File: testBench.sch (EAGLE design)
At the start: 29 parts, among them IC1 NCS21911SN2T1G, IC2 NCS21911SN2T1G, IC3 NCS21911SN2T1G, IC4 NCS21911SN2T1G, IC5 NCS21911SN2T1G

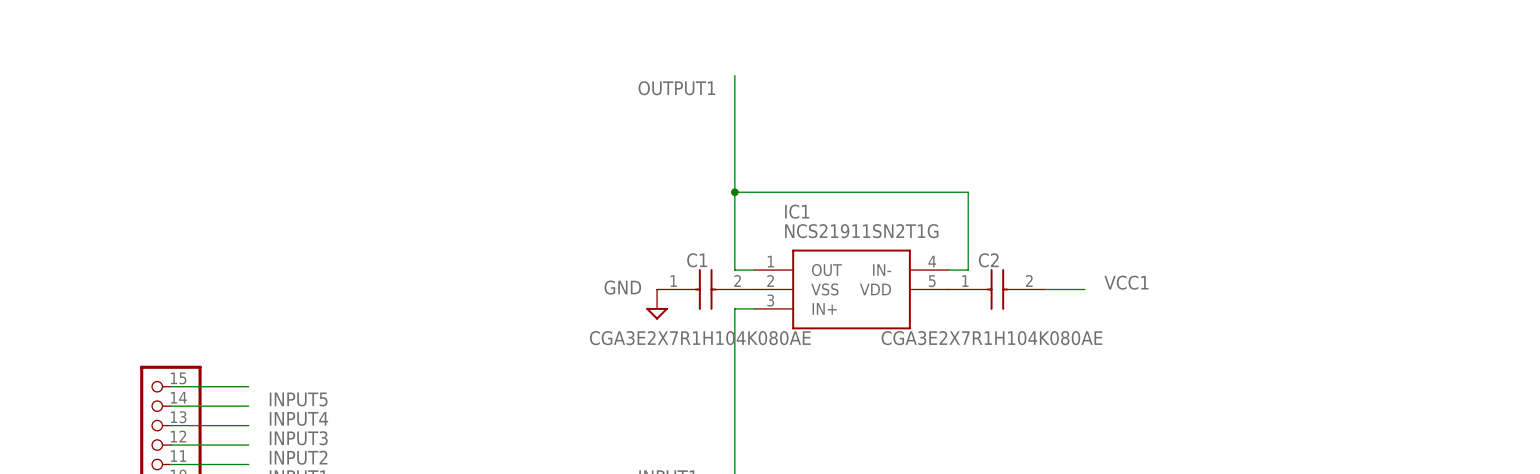
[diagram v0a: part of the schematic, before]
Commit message: Added comments on schematics
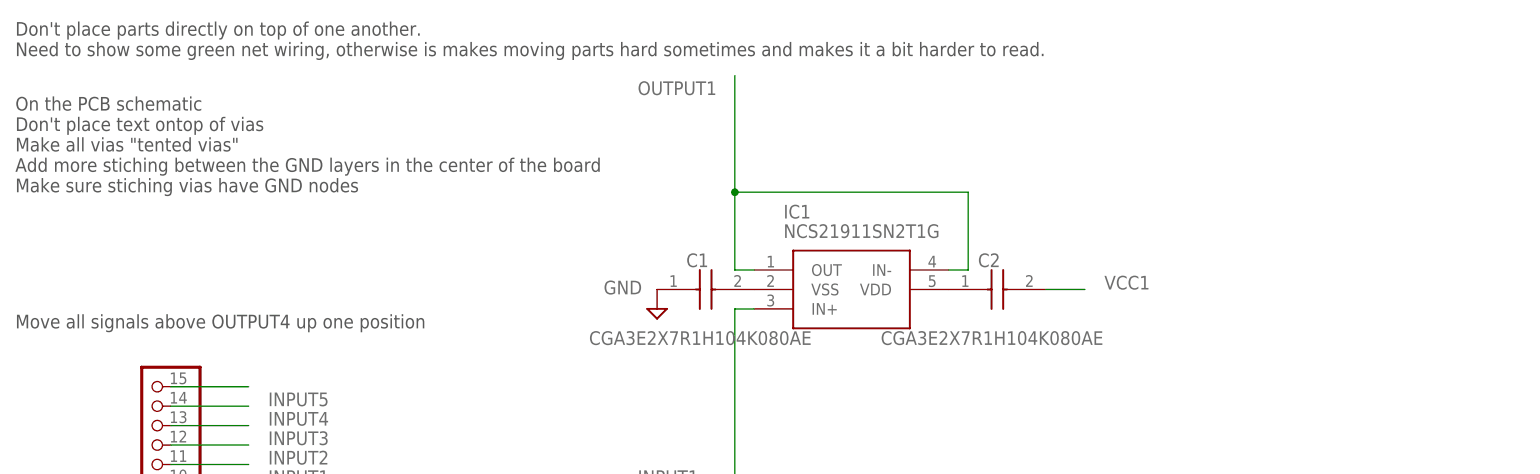
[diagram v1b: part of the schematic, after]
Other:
- note added: "Don't place parts directly on top of one another. Need to show some green net wiring, otherwise is makes moving parts hard sometimes and makes it a bit harder to read."
- note added: "Move all signals above OUTPUT4 up one position"
- note added: "On the PCB schematic Don't place text ontop of vias Make all vias "tented vias" Add more stiching between the GND layers in the center of the board Make sure stiching vias have GND nodes"
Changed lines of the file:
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@@
 <text x="124.46" y="-104.14" size="5.08" layer="97">Second-order Low-pass Filter</text>
 <text x="124.46" y="-238.76" size="5.08" layer="97">Differential Amplifier</text>
+<text x="-127" y="30.48" size="1.778" layer="97">Move all signals above OUTPUT4 up one position</text>
+<text x="-127" y="66.04" size="1.778" layer="97">Don't place parts directly on top of one another.
+Need to show some green net wiring, otherwise is makes moving parts hard sometimes and makes it a bit harder to read.</text>
+<text x="-127" y="48.26" size="1.778" layer="97">On the PCB schematic
+Don't place text ontop of vias
+Make all vias "tented vias"
+Add more stiching between the GND layers in the center of the board
+Make sure stiching vias have GND nodes</text>
 </plain>
 <instances>
@@
 </drawing>
 <compatibility>
+<note version="6.3" minversion="6.2.2" severity="warning">
+Since Version 6.2.2 text objects can contain more than one line,
+which will not be processed correctly with this version.
+</note>
 <note version="8.2" severity="warning">
 Since Version 8.2, EAGLE supports online libraries. The ids

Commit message: This is my third PCB for opamp test bench
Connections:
- removed net N$44: JP3.15
- new net EMPTY: JP3.5
- net GND: now also JP3.10; no longer JP3.9
- net INPUT1: now also JP3.11; no longer JP3.10
- net INPUT2: now also JP3.12; no longer JP3.11
- net INPUT3: now also JP3.13; no longer JP3.12
- net INPUT4: now also JP3.14; no longer JP3.13
- net INPUT5: now also JP3.15; no longer JP3.14
- net VCC1: now also JP3.6; no longer JP3.5
- net VCC2: now also JP3.7; no longer JP3.6
- net VCC3: now also JP3.8; no longer JP3.7
- net VCC4: now also JP3.9; no longer JP3.8
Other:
- moved on the sheet: C1, C10, C11, C12, C13, C2, C3, C4, C6, C7

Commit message: PCB test bench fourth version
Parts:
- removed C1, C10, C12, C3, C6: CGA3E2X7R1H104K080AE, SamacSys_Parts:CGA3E2X7R1H104K080AE
- added TP1, TP2, TP3, TP4, TP5, TP6, TP7, TP8: (no value), SamacSys_Parts:S1751-46R
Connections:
- removed net N$16: C11.1, IC5.VDD
- removed net N$17: C10.2, IC5.VSS
- removed net N$2: C1.2, IC1.VSS
- removed net N$3: C2.1, IC1.VDD
- removed net N$4: C3.2, IC2.VSS
- removed net N$5: C4.1, IC2.VDD
- removed net N$6: C6.2, IC3.VSS
- removed net N$7: C7.1, IC3.VDD
- removed net N$8: C13.1, IC4.VDD
- removed net N$9: C12.2, IC4.VSS
- net GND: now also C11.2, C13.2, C2.2, C4.2, C7.2, IC1.VSS, IC2.VSS, IC3.VSS, IC4.VSS, IC5.VSS, TP1.TP, TP3.TP, TP5.TP, TP7.TP; no longer C1.1, C10.1, C12.1, C3.1, C6.1
- net OUTPUT1: now also TP2.TP
- net OUTPUT2: now also TP4.TP
- net OUTPUT3: now also TP6.TP
- net OUTPUT4: now also TP8.TP
- net VCC1: now also C2.1, IC1.VDD; no longer C2.2
- net VCC2: now also C4.1, IC2.VDD; no longer C4.2
- net VCC3: now also C11.1, C7.1, IC3.VDD, IC5.VDD; no longer C11.2, C7.2
- net VCC4: now also C13.1, IC4.VDD; no longer C13.2
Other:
- moved on the sheet: C11, C13, C2, C4, C7, C8

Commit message: pcb test bench 6th version
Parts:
- removed R6: CRCW080510M0FKEB, SamacSys_Parts:CRCW080510M0FKEB
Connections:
- removed net N$18: IC5.OUT, R6.1, R7.1
- net OUTPUT3: now also IC5.OUT, R7.1; no longer R6.2
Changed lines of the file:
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@@
 <part name="C11" library="SamacSys_Parts" deviceset="CGA3E2X7R1H104K080AE" device=""/>
 <part name="SUPPLY10" library="supply2" library_urn="urn:adsk.eagle:library:372" deviceset="GND" device=""/>
-<part name="R6" library="SamacSys_Parts" deviceset="CRCW080510M0FKEB" device=""/>
 <part name="SUPPLY13" library="supply2" library_urn="urn:adsk.eagle:library:372" deviceset="GND" device=""/>
 <part name="R8" library="SamacSys_Parts" deviceset="TNPW080510K0BEEN" device=""/>
@@
 <attribute name="VALUE" x="36.195" y="-140.335" size="1.778" layer="96"/>
 </instance>
-<instance part="R6" gate="G$1" x="43.18" y="-93.98" smashed="yes" rot="R90">
-<attribute name="NAME" x="36.83" y="-82.55" size="1.778" layer="95" rot="R180" align="center-left"/>
-<attribute name="VALUE" x="39.37" y="-87.63" size="1.778" layer="96" rot="R180" align="center-left"/>
-</instance>
 <instance part="SUPPLY13" gate="GND" x="-5.08" y="-139.7" smashed="yes" rot="R90">
 <attribute name="VALUE" x="1.905" y="-139.065" size="1.778" layer="96" rot="R180"/>
@@
 </segment>
 </net>
-<net name="N$18" class="0">
-<segment>
+<net name="OUTPUT3" class="0">
+<segment>
+<label x="48.26" y="-66.04" size="1.778" layer="95" rot="R180"/>
 <pinref part="IC5" gate="G$1" pin="OUT"/>
-<pinref part="R6" gate="G$1" pin="1"/>
 <wire x1="43.18" y1="-121.92" x2="43.18" y2="-104.14" width="0.1524" layer="91"/>
 <pinref part="R7" gate="G$1" pin="1"/>
-<wire x1="43.18" y1="-104.14" x2="43.18" y2="-93.98" width="0.1524" layer="91"/>
 <wire x1="43.18" y1="-104.14" x2="45.72" y2="-104.14" width="0.1524" layer="91"/>
 <junction x="43.18" y="-104.14"/>
-</segment>
-</net>
-<net name="OUTPUT3" class="0">
-<segment>
-<pinref part="R6" gate="G$1" pin="2"/>
-<wire x1="43.18" y1="-76.2" x2="43.18" y2="-71.12" width="0.1524" layer="91"/>
-<label x="48.26" y="-66.04" size="1.778" layer="95" rot="R180"/>
-</segment>
-<segment>
+<wire x1="43.18" y1="-71.12" x2="43.18" y2="-104.14" width="0.1524" layer="91"/>
+</segment>
+<segment>

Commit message: PCB test bench version 8th
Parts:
- added LED1, LED2, LED3, LED4: 150080GS75000, SamacSys_Parts:150080GS75000
- added R13, R14, R15, R16: ERJ-P06J431V, SamacSys_Parts:ERJ-P06J431V
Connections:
- new net N$23: LED1.A, R13.2
- new net N$30: LED2.A, R14.2
- new net N$31: LED3.A, R15.2
- new net N$32: LED4.A, R16.2
- net GND: now also LED1.K, LED2.K, LED3.K, LED4.K
- net VCC1: now also R13.1
- net VCC2: now also R14.1
- net VCC3: now also R15.1
- net VCC4: now also R16.1
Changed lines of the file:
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@@
 <part name="TP7" library="SamacSys_Parts" deviceset="S1751-46R" device=""/>
 <part name="TP8" library="SamacSys_Parts" deviceset="S1751-46R" device=""/>
+<part name="LED1" library="SamacSys_Parts" deviceset="150080GS75000" device=""/>
+<part name="R13" library="SamacSys_Parts" deviceset="ERJ-P06J431V" device=""/>
+<part name="SUPPLY15" library="supply2" library_urn="urn:adsk.eagle:library:372" deviceset="GND" device=""/>
+<part name="LED2" library="SamacSys_Parts" deviceset="150080GS75000" device=""/>
+<part name="R14" library="SamacSys_Parts" deviceset="ERJ-P06J431V" device=""/>
+<part name="SUPPLY16" library="supply2" library_urn="urn:adsk.eagle:library:372" deviceset="GND" device=""/>
+<part name="LED3" library="SamacSys_Parts" deviceset="150080GS75000" device=""/>
+<part name="R15" library="SamacSys_Parts" deviceset="ERJ-P06J431V" device=""/>
+<part name="SUPPLY17" library="supply2" library_urn="urn:adsk.eagle:library:372" deviceset="GND" device=""/>
+<part name="LED4" library="SamacSys_Parts" deviceset="150080GS75000" device=""/>
+<part name="R16" library="SamacSys_Parts" deviceset="ERJ-P06J431V" device=""/>
+<part name="SUPPLY18" library="supply2" library_urn="urn:adsk.eagle:library:372" deviceset="GND" device=""/>
 </parts>
 <sheets>
@@
 <attribute name="NAME" x="53.34" y="-256.54" size="1.27" layer="95" rot="R270"/>
 </instance>
+<instance part="LED1" gate="G$1" x="-172.72" y="22.86" smashed="yes" rot="R180">
+<attribute name="NAME" x="-167.64" y="31.75" size="1.778" layer="95" rot="R180"/>
+<attribute name="VALUE" x="-167.64" y="29.21" size="1.778" layer="96" rot="R180"/>
+</instance>
+<instance part="R13" gate="G$1" x="-220.98" y="22.86" smashed="yes">
+<attribute name="NAME" x="-207.01" y="29.21" size="1.778" layer="95" align="center-left"/>
+<attribute name="VALUE" x="-207.01" y="26.67" size="1.778" layer="96" align="center-left"/>
+</instance>
+<instance part="SUPPLY15" gate="GND" x="-157.48" y="22.86" smashed="yes" rot="R90">
+<attribute name="VALUE" x="-150.495" y="23.495" size="1.778" layer="96" rot="R180"/>
+</instance>
+<instance part="LED2" gate="G$1" x="-172.72" y="10.16" smashed="yes" rot="R180">
+<attribute name="NAME" x="-167.64" y="19.05" size="1.778" layer="95" rot="R180"/>
+<attribute name="VALUE" x="-167.64" y="16.51" size="1.778" layer="96" rot="R180"/>
+</instance>
+<instance part="R14" gate="G$1" x="-220.98" y="10.16" smashed="yes">
+<attribute name="NAME" x="-207.01" y="16.51" size="1.778" layer="95" align="center-left"/>
+<attribute name="VALUE" x="-207.01" y="13.97" size="1.778" layer="96" align="center-left"/>
+</instance>
+<instance part="SUPPLY16" gate="GND" x="-157.48" y="10.16" smashed="yes" rot="R90">
+<attribute name="VALUE" x="-150.495" y="10.795" size="1.778" layer="96" rot="R180"/>
+</instance>
+<instance part="LED3" gate="G$1" x="-172.72" y="-2.54" smashed="yes" rot="R180">
+<attribute name="NAME" x="-167.64" y="6.35" size="1.778" layer="95" rot="R180"/>
+<attribute name="VALUE" x="-167.64" y="3.81" size="1.778" layer="96" rot="R180"/>
+</instance>
+<instance part="R15" gate="G$1" x="-220.98" y="-2.54" smashed="yes">
+<attribute name="NAME" x="-207.01" y="3.81" size="1.778" layer="95" align="center-left"/>
+<attribute name="VALUE" x="-207.01" y="1.27" size="1.778" layer="96" align="center-left"/>
+</instance>
+<instance part="SUPPLY17" gate="GND" x="-157.48" y="-2.54" smashed="yes" rot="R90">
+<attribute name="VALUE" x="-150.495" y="-1.905" size="1.778" layer="96" rot="R180"/>
+</instance>
+<instance part="LED4" gate="G$1" x="-172.72" y="-15.24" smashed="yes" rot="R180">
+<attribute name="NAME" x="-167.64" y="-6.35" size="1.778" layer="95" rot="R180"/>
+<attribute name="VALUE" x="-167.64" y="-8.89" size="1.778" layer="96" rot="R180"/>
+</instance>
+<instance part="R16" gate="G$1" x="-220.98" y="-15.24" smashed="yes">
+<attribute name="NAME" x="-207.01" y="-8.89" size="1.778" layer="95" align="center-left"/>
+<attribute name="VALUE" x="-207.01" y="-11.43" size="1.778" layer="96" align="center-left"/>
+</instance>
+<instance part="SUPPLY18" gate="GND" x="-157.48" y="-15.24" smashed="yes" rot="R90">
+<attribute name="VALUE" x="-150.495" y="-14.605" size="1.778" layer="96" rot="R180"/>
+</instance>
 </instances>
 <busses>
@@
 <wire x1="68.58" y1="-243.84" x2="76.2" y2="-243.84" width="0.1524" layer="91"/>
 <label x="78.74" y="-243.84" size="1.778" layer="95"/>
+</segment>
+<segment>
+<pinref part="LED1" gate="G$1" pin="K"/>
+<wire x1="-172.72" y1="22.86" x2="-160.02" y2="22.86" width="0.1524" layer="91"/>
+<pinref part="SUPPLY15" gate="GND" pin="GND"/>
+</segment>
+<segment>
+<pinref part="LED2" gate="G$1" pin="K"/>
+<wire x1="-172.72" y1="10.16" x2="-160.02" y2="10.16" width="0.1524" layer="91"/>
+<pinref part="SUPPLY16" gate="GND" pin="GND"/>
+</segment>
+<segment>
+<pinref part="LED3" gate="G$1" pin="K"/>
+<wire x1="-172.72" y1="-2.54" x2="-160.02" y2="-2.54" width="0.1524" layer="91"/>
+<pinref part="SUPPLY17" gate="GND" pin="GND"/>
+</segment>
+<segment>
+<pinref part="LED4" gate="G$1" pin="K"/>
+<wire x1="-172.72" y1="-15.24" x2="-160.02" y2="-15.24" width="0.1524" layer="91"/>
+<pinref part="SUPPLY18" gate="GND" pin="GND"/>
 </segment>
 </net>
@@
 <label x="25.4" y="-233.68" size="1.778" layer="95"/>
 </segment>
+<segment>
+<pinref part="R16" gate="G$1" pin="1"/>
+<wire x1="-220.98" y1="-15.24" x2="-233.68" y2="-15.24" width="0.1524" layer="91"/>
+<label x="-241.3" y="-15.24" size="1.778" layer="95"/>
+</segment>
 </net>
 <net name="VCC3" class="0">
@@
 <label x="10.16" y="-124.46" size="1.778" layer="95"/>
 </segment>
+<segment>
+<pinref part="R15" gate="G$1" pin="1"/>
+<wire x1="-220.98" y1="-2.54" x2="-233.68" y2="-2.54" width="0.1524" layer="91"/>
+<label x="-241.3" y="-2.54" size="1.778" layer="95"/>
+</segment>
 </net>
 <net name="VCC2" class="0">
@@
 <label x="22.86" y="-30.48" size="1.778" layer="95"/>
 </segment>
+<segment>
+<pinref part="R14" gate="G$1" pin="1"/>
+<wire x1="-220.98" y1="10.16" x2="-233.68" y2="10.16" width="0.1524" layer="91"/>
+<label x="-241.3" y="10.16" size="1.778" layer="95"/>
+</segment>
 </net>
 <net name="VCC1" class="0">
@@
 <label x="15.24" y="35.56" size="1.778" layer="95"/>
 </segment>
+<segment>
+<pinref part="R13" gate="G$1" pin="1"/>
+<wire x1="-220.98" y1="22.86" x2="-233.68" y2="22.86" width="0.1524" layer="91"/>
+<label x="-241.3" y="22.86" size="1.778" layer="95"/>
+</segment>
 </net>
 <net name="EMPTY" class="0">
@@
 </segment>
 </net>
+<net name="N$23" class="0">
+<segment>
+<pinref part="R13" gate="G$1" pin="2"/>
+<pinref part="LED1" gate="G$1" pin="A"/>
+<wire x1="-203.2" y1="22.86" x2="-187.96" y2="22.86" width="0.1524" layer="91"/>
+</segment>
+</net>
+<net name="N$30" class="0">
+<segment>
+<pinref part="R14" gate="G$1" pin="2"/>
+<pinref part="LED2" gate="G$1" pin="A"/>
+<wire x1="-203.2" y1="10.16" x2="-187.96" y2="10.16" width="0.1524" layer="91"/>
+</segment>
+</net>
+<net name="N$31" class="0">
+<segment>
+<pinref part="R15" gate="G$1" pin="2"/>
+<pinref part="LED3" gate="G$1" pin="A"/>
+<wire x1="-203.2" y1="-2.54" x2="-187.96" y2="-2.54" width="0.1524" layer="91"/>
+</segment>
+</net>
+<net name="N$32" class="0">
+<segment>
+<pinref part="R16" gate="G$1" pin="2"/>
+<pinref part="LED4" gate="G$1" pin="A"/>
+<wire x1="-203.2" y1="-15.24" x2="-187.96" y2="-15.24" width="0.1524" layer="91"/>
+</segment>
+</net>
